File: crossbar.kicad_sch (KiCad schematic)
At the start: 32 parts

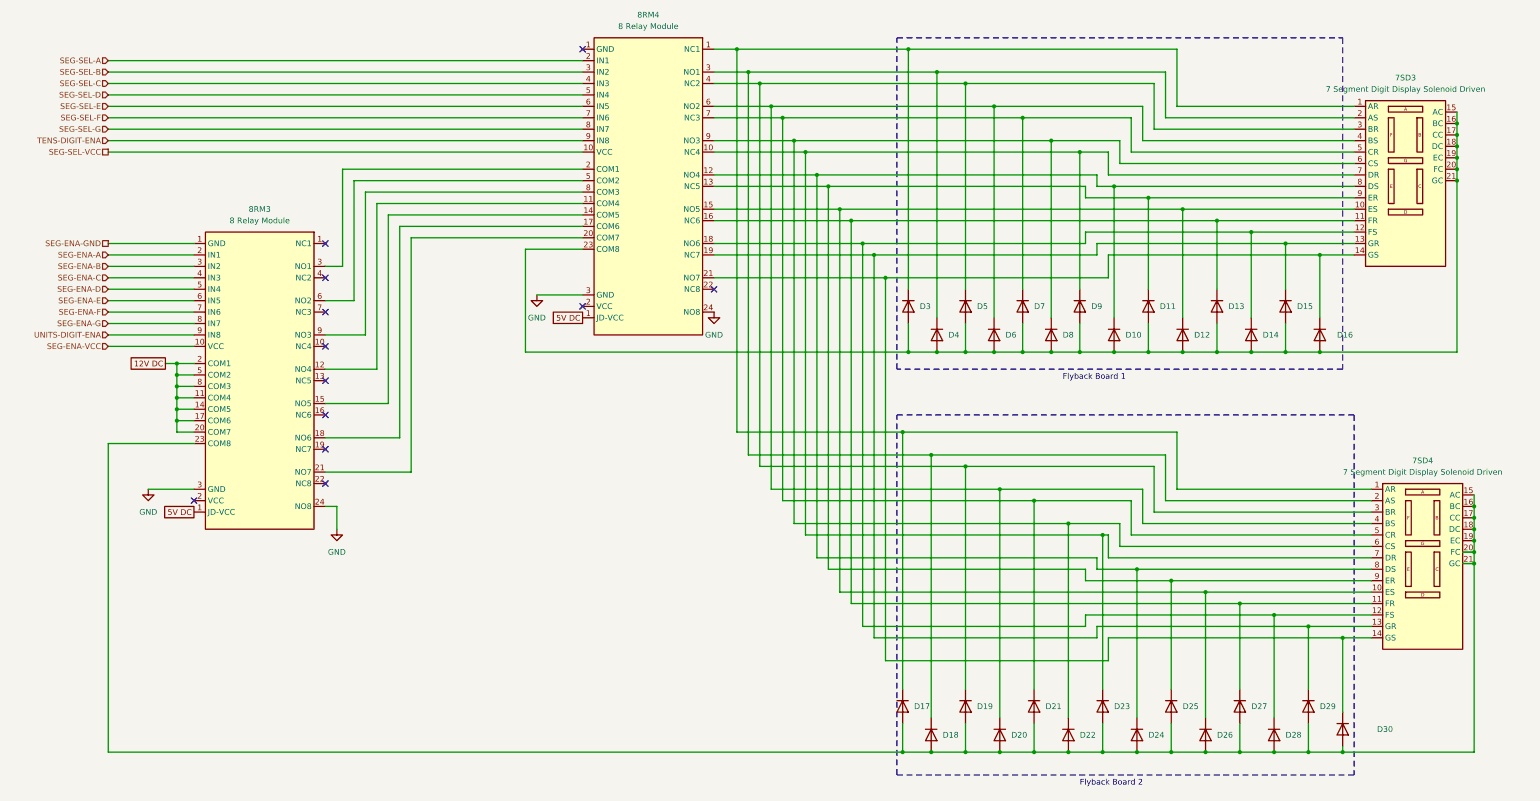
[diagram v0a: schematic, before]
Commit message: changes to mechanical drawings
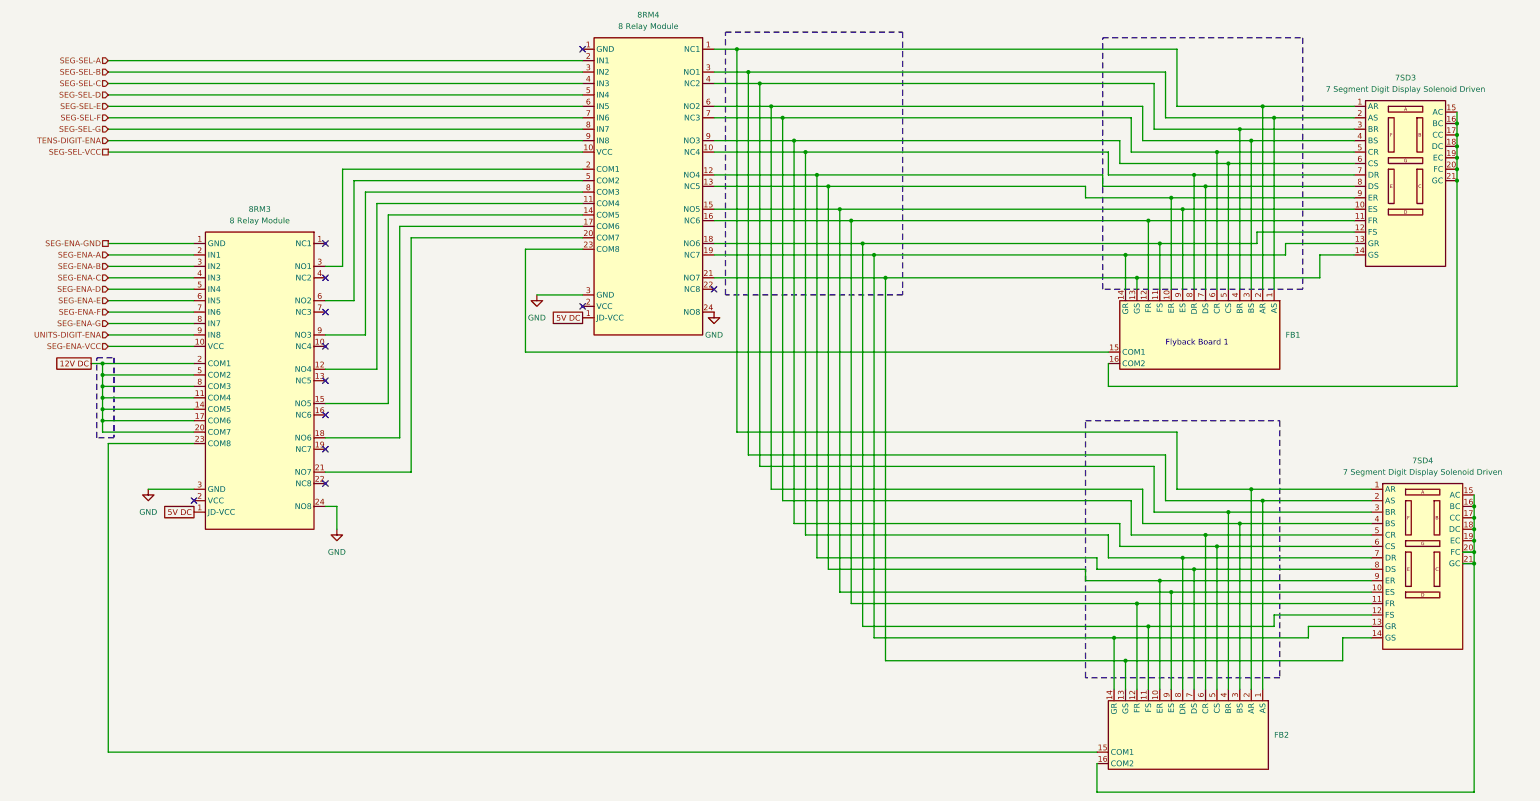
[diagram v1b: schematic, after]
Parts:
- removed D10, D11, D12, D13, D14, D15, D16, D17, D18, D19, D20, D21, D22, D23, D24, D25, D26, D27, D28, D29, D3, D30, D4, D5, D6, D7, D8, D9: 1N4007, Diode_THT:D_DO-41_SOD81_P10.16mm_Horizontal, symbol Diode:1N4007
- added FB1, FB2: ~, symbol Project Library:Flyback_Board
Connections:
- net at 7SD3.7 (DR), 7SD4.7 (DR), 8RM4.10 (VCC): now also FB1.8 (DR), FB2.8 (DR)
- net at 7SD4.15 (AC), 7SD4.16 (BC), 7SD4.17 (CC)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: now also FB2.16 (COM2); no longer 8RM3.23 (COM8)
- net at 7SD3.5 (CR), 7SD4.5 (CR), 8RM4.7 (NC3): now also FB1.6 (CR), FB2.6 (CR)
- net at 7SD3.15 (AC), 7SD3.16 (BC), 7SD3.17 (CC)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: now also FB1.16 (COM2); no longer 8RM4.23 (COM8)
- net at 7SD3.9 (ER), 7SD4.9 (ER), 8RM4.13 (NC5): now also FB1.10 (ER), FB2.10 (ER)
- net at 7SD3.14 (GS), 7SD4.14 (GS), 8RM4.21 (NO7): now also FB1.13 (GS), FB2.13 (GS)
- net at 7SD3.3 (BR), 7SD4.3 (BR), 8RM4.4 (NC2): now also FB1.4 (BR), FB2.4 (BR)
- net at 7SD3.2 (AS), 7SD4.2 (AS), 8RM4.3 (NO1): now also FB1.1 (AS), FB2.1 (AS)
- net at 7SD3.4 (BS), 7SD4.4 (BS), 8RM4.6 (NO2): now also FB1.3 (BS), FB2.3 (BS)
- net at 7SD3.11 (FR), 7SD4.11 (FR), 8RM4.16 (NC6): now also FB1.12 (FR), FB2.12 (FR)
- net at 7SD3.1 (AR), 7SD4.1 (AR), 8RM4.1 (NC1): now also FB1.2 (AR), FB2.2 (AR)
- net at 7SD3.13 (GR), 7SD4.13 (GR), 8RM4.19 (NC7): now also FB1.14 (GR), FB2.14 (GR)
- net at 7SD3.12 (FS), 7SD4.12 (FS), 8RM4.18 (NO6): now also FB1.11 (FS), FB2.11 (FS)
- net at 7SD3.6 (CS), 7SD4.6 (CS), 8RM4.9 (NO3): now also FB1.5 (CS), FB2.5 (CS)
- net at 7SD3.8 (DS), 7SD4.8 (DS), 8RM4.12 (NO4): now also FB1.7 (DS), FB2.7 (DS)
- net at 7SD3.10 (ES), 7SD4.10 (ES), 8RM4.15 (NO5): now also FB1.9 (ES), FB2.9 (ES)
- new net: 8RM4.23 (COM8), FB1.15 (COM1)
- new net: 8RM3.23 (COM8), FB2.15 (COM1)
- new net: 8RM3.3 (NO1), 8RM4.2 (VCC)
- new net: 8RM3.6 (NO2), 8RM4.5 (IN4)
- new net: 8RM3.9 (NO3), 8RM4.8 (IN7)
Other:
- note removed: "Flyback Board 2"

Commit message: lots of diagram changes and software dir.
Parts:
- removed FB1, FB2: ~, symbol Project Library:Flyback_Board
- added FB1: ~, symbol Project Library:Flyback_Board_3
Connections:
- net at 8RM4.23 (COM8): now also FB1.45 (UC1)
- net at 7SD3.15 (AC), 7SD3.16 (BC), 7SD3.17 (CC)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: now also FB1.46 (UC2)
- net at 8RM3.23 (COM8): now also FB1.43 (TC1)
- net at 7SD4.15 (AC), 7SD4.16 (BC), 7SD4.17 (CC)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: now also FB1.44 (TC2)
- new net: 8RM3.3 (NO1), 8RM4.2 (VCC)
- new net: 8RM3.6 (NO2), 8RM4.5 (IN4)
- new net: 8RM3.9 (NO3), 8RM4.8 (IN7)
- new net: 8RM4.1 (NC1), FB1.1 (AR)
- new net: 8RM4.10 (VCC), FB1.7 (DR)
- new net: 8RM4.12 (NO4), FB1.8 (DS)
- new net: 8RM4.13 (NC5), FB1.9 (ER)
- new net: 8RM4.15 (NO5), FB1.10 (ES)
- new net: 8RM4.16 (NC6), FB1.11 (FR)
- new net: 8RM4.18 (NO6), FB1.12 (FS)
- new net: 8RM4.19 (NC7), FB1.13 (GR)
- new net: 8RM4.21 (NO7), FB1.14 (GS)
- new net: 8RM4.3 (NO1), FB1.2 (AS)
- new net: 8RM4.4 (NC2), FB1.3 (BR)
- new net: 8RM4.6 (NO2), FB1.4 (BS)
- new net: 8RM4.7 (NC3), FB1.5 (CR)
- new net: 8RM4.9 (NO3), FB1.6 (CS)
- new net: 7SD4.1 (AR), FB1.16 (UAR)
- new net: 7SD4.10 (ES), FB1.34 (UES)
- new net: 7SD4.11 (FR), FB1.36 (UFR)
- new net: 7SD4.12 (FS), FB1.38 (UFS)
- new net: 7SD4.13 (GR), FB1.40 (UGR)
- new net: 7SD4.14 (GS), FB1.42 (UGS)
- new net: 7SD4.2 (AS), FB1.18 (UAS)
- new net: 7SD4.3 (BR), FB1.20 (UBR)
- new net: 7SD4.4 (BS), FB1.22 (UBS)
- new net: 7SD4.5 (CR), FB1.24 (UCR)
- new net: 7SD4.6 (CS), FB1.26 (UCS)
- new net: 7SD4.7 (DR), FB1.28 (UDR)
- new net: 7SD4.8 (DS), FB1.30 (UDS)
- new net: 7SD4.9 (ER), FB1.32 (UER)
- new net: 7SD3.1 (AR), FB1.15 (TAR)
- new net: 7SD3.10 (ES), FB1.33 (TES)
- new net: 7SD3.11 (FR), FB1.35 (TFR)
- new net: 7SD3.12 (FS), FB1.37 (TFS)
- new net: 7SD3.13 (GR), FB1.39 (TGR)
- new net: 7SD3.14 (GS), FB1.41 (TGS)
- new net: 7SD3.2 (AS), FB1.17 (TAS)
- new net: 7SD3.3 (BR), FB1.19 (TBR)
- new net: 7SD3.4 (BS), FB1.21 (TBS)
- new net: 7SD3.5 (CR), FB1.23 (TCR)
- new net: 7SD3.6 (CS), FB1.25 (TCS)
- new net: 7SD3.7 (DR), FB1.27 (TDR)
- new net: 7SD3.8 (DS), FB1.29 (TDS)
- new net: 7SD3.9 (ER), FB1.31 (TER)
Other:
- note removed: "Flyback Board 1"
- moved on the sheet: 7SD3

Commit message: Misc clean up
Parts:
- renumbered 7SD3 to 7SD1, 7SD4 to 7SD2, 8RM4 to 8RM1, 8RM3 to 8RM2
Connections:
- new net: 8RM1.2 (VCC), 8RM2.3 (NO1)
- new net: 8RM1.5 (IN4), 8RM2.6 (NO2)
- new net: 8RM1.8 (IN7), 8RM2.9 (NO3)
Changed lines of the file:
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@@
   (symbol (lib_id "Project Library:8_Relay_Module_B") (at 101.6 119.38 270) (unit 1)
     (in_bom yes) (on_board yes) (dnp no) (fields_autoplaced)
-    (property "Reference" "8RM3" (at 85.725 81.28 90)
+    (property "Reference" "8RM2" (at 85.725 81.28 90)
       (effects (font (size 1.27 1.27)))
     )
@@
       (project "NCNCA-Lap_Counter"
         (path "/f7d7cc02-a4fd-4b7a-92a3-de67af0c24a1/5a0f4047-acb5-4a8c-b6a8-12c7c3c67579"
-          (reference "8RM3") (unit 1)
+          (reference "8RM2") (unit 1)
         )
       )
@@
   (symbol (lib_id "Project Library:8_Relay_Module_B") (at 187.96 76.2 270) (unit 1)
     (in_bom yes) (on_board yes) (dnp no) (fields_autoplaced)
-    (property "Reference" "8RM4" (at 172.085 38.1 90)
+    (property "Reference" "8RM1" (at 172.085 38.1 90)
       (effects (font (size 1.27 1.27)))
     )
@@
       (project "NCNCA-Lap_Counter"
         (path "/f7d7cc02-a4fd-4b7a-92a3-de67af0c24a1/5a0f4047-acb5-4a8c-b6a8-12c7c3c67579"
-          (reference "8RM4") (unit 1)
+          (reference "8RM1") (unit 1)
         )
       )
@@
   (symbol (lib_id "Project Library:7_Segment_Solenoid") (at 344.17 139.7 0) (unit 1)
     (in_bom yes) (on_board yes) (dnp no) (fields_autoplaced)
-    (property "Reference" "7SD4" (at 344.17 137.16 0)
+    (property "Reference" "7SD2" (at 344.17 137.16 0)
       (effects (font (size 1.27 1.27)))
     )
@@
       (project "NCNCA-Lap_Counter"
         (path "/f7d7cc02-a4fd-4b7a-92a3-de67af0c24a1/5a0f4047-acb5-4a8c-b6a8-12c7c3c67579"
-          (reference "7SD4") (unit 1)
+          (reference "7SD2") (unit 1)
         )
       )
@@
   (symbol (lib_name "7_Segment_Solenoid_1") (lib_id "Project Library:7_Segment_Solenoid") (at 340.36 40.64 0) (unit 1)
     (in_bom yes) (on_board yes) (dnp no) (fields_autoplaced)
-    (property "Reference" "7SD3" (at 340.36 38.1 0)
+    (property "Reference" "7SD1" (at 340.36 38.1 0)
       (effects (font (size 1.27 1.27)))
     )
@@
       (project "NCNCA-Lap_Counter"
         (path "/f7d7cc02-a4fd-4b7a-92a3-de67af0c24a1/5a0f4047-acb5-4a8c-b6a8-12c7c3c67579"
-          (reference "7SD3") (unit 1)
-        )
-      )
+          (reference "7SD1") (unit 1)
+        )
+      )

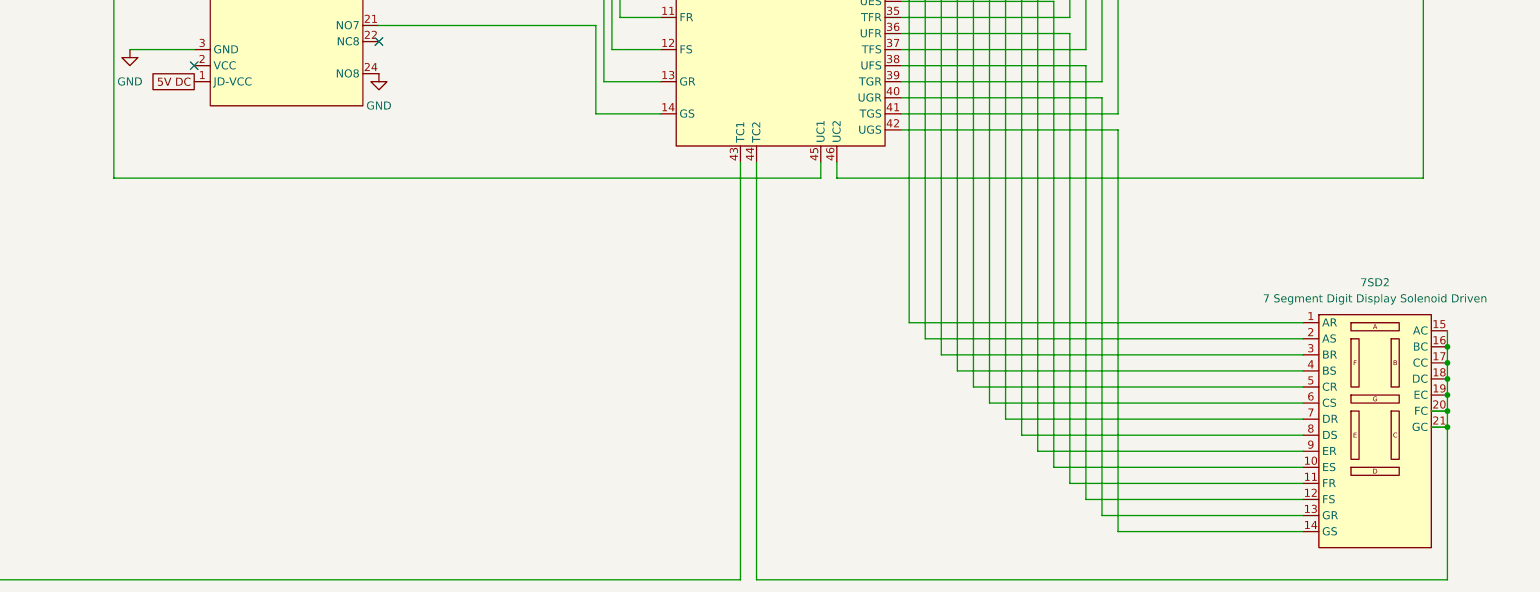
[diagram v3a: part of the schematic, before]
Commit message: eliminate over-large mp4 file
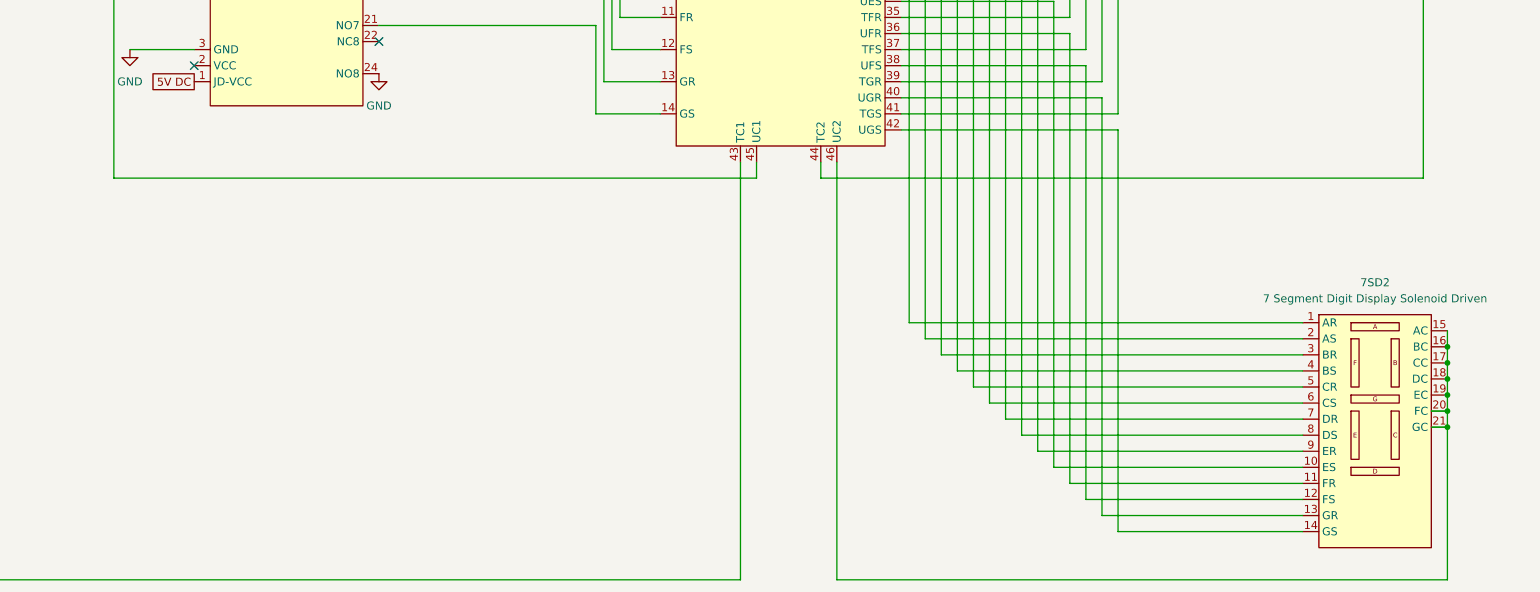
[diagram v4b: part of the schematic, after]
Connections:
- net at 7SD2.15 (AC), 7SD2.16 (BC), 7SD2.17 (CC)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: now also FB1.46 (UC2); no longer FB1.44 (TC2)
- net at 7SD1.15 (AC), 7SD1.16 (BC), 7SD1.17 (CC)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: now also FB1.44 (TC2); no longer FB1.46 (UC2)
- new net: 8RM1.2 (VCC), 8RM2.3 (NO1)
- new net: 8RM1.5 (IN4), 8RM2.6 (NO2)
- new net: 8RM1.8 (IN7), 8RM2.9 (NO3)
